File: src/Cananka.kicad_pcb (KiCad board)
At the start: 2 copper layers, 105.8 x 26 mm, 50 parts, among them J1 USB4085 B1HSW6, J2 MC 1,5/4, Q1 DMP3085, U1 FT230XS, U2 PIC18F25K80, U3 ISO1050, U4 PC817C, Y1 12 MHz

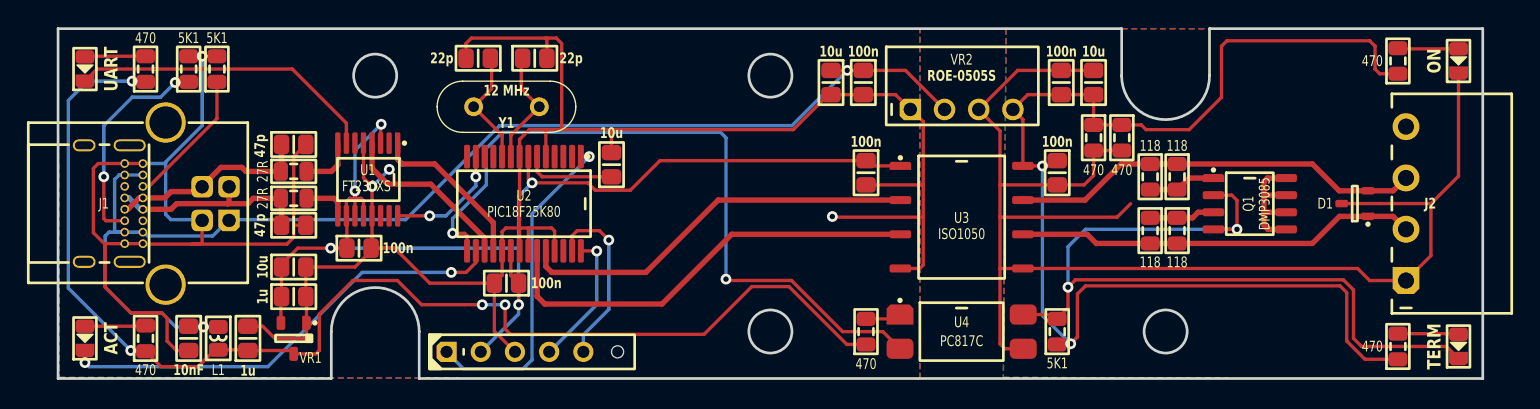
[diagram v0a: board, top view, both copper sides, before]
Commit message: Added soft-start circuit for DC-DC converter
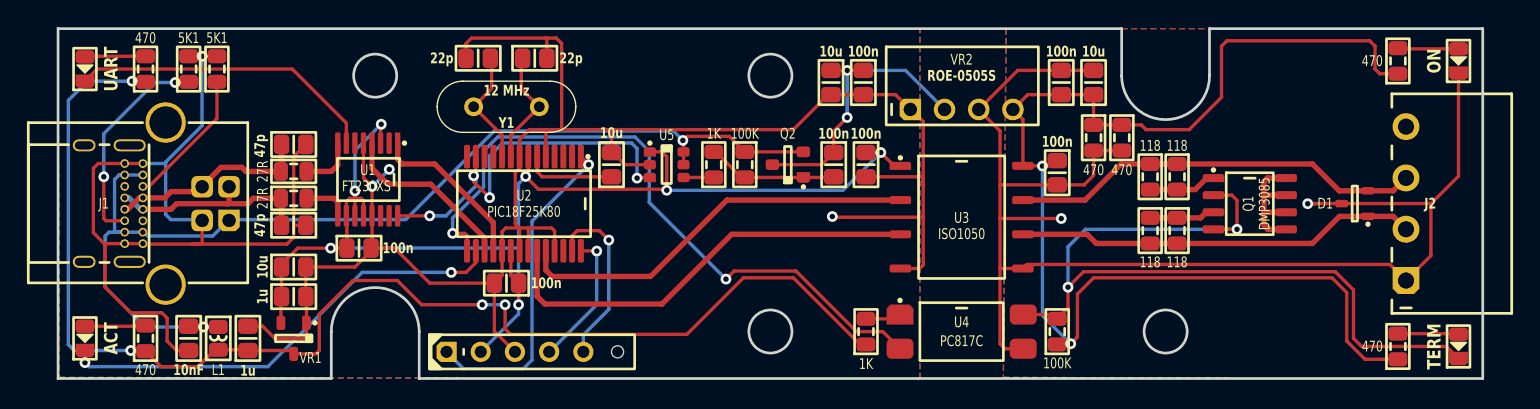
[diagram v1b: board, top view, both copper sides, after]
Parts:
- added C12: 100n, Medo64:C (0805), F.Cu at (77.6, 30.1)
- added Q2: Val**, Medo64:Q MOSFET-P (SOT23-3), F.Cu at (74.2, 30.1)
- added R14: 1K, Medo64:R (0805), F.Cu at (68.7, 30.1)
- added R18: 100K, Medo64:R (0805), F.Cu at (71.0, 30.1)
- added U5: 74LVC1T45, Medo64:U LevelTranslator [74LVC1T45] (SOT23-6), F.Cu at (65.2, 30.1)
- R17: renamed from R16; value 5K1 -> 100K
- R7: value 470 -> 1K
- moved C8 0.60 mm to (80.0, 30.1)
- renumbered C12 to C13, C13 to C14, C14 to C15, C15 to C16, C16 to C17, C17 to C18, R14 to R15, R15 to R16, R8 to R7, R9 to R8
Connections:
- C10 pad 1: A_5V_USB -> A_5V_SWITCHED
- C17 pad 1: A_5V_USB -> A_5V_SWITCHED
- VR2 pad 2: A_5V_USB -> A_5V_SWITCHED
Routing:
- net A_5V_SWITCHED: track 0.00 -> 22.3 mm, vias 0 -> 2
- net A_PWREN#: track 8.82 -> 28.7 mm, vias 2 -> 4
- net A_5V_USB: track 91.4 -> 79.4 mm
- net A_PWREN#_5V': track 0.00 -> 9.04 mm
- net A_3V3: track 86.9 -> 92.9 mm, vias 5 -> 7
- net A_GND: track 202.5 -> 206.4 mm
- net A_IO_TERMINATE#: track 53.6 -> 49.9 mm
- net A_5V: track 92.1 -> 94.6 mm
- net A_PWREN#_5V: track 0.00 -> 2.25 mm
- net B_GND: track 105.1 -> 102.9 mm, vias 0 -> 2
- net B_CAN_L_SPLIT: track 4.97 -> 4.44 mm

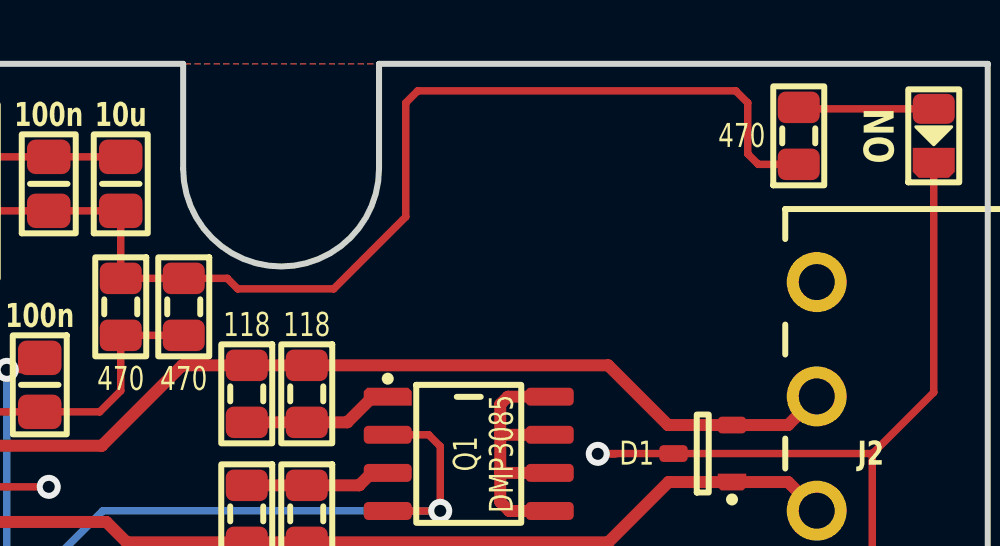
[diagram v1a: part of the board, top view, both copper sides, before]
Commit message: Added testing V+ output
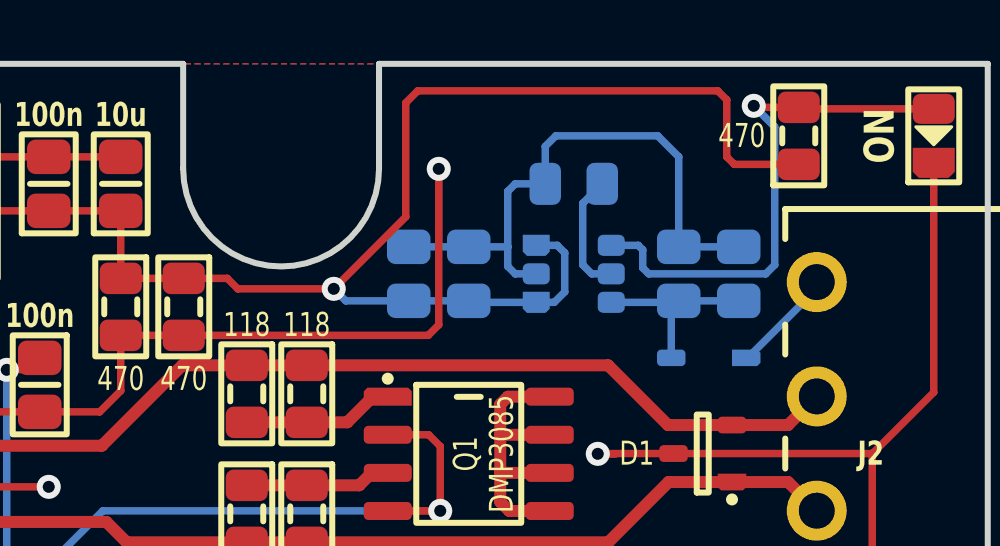
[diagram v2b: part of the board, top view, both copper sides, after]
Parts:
- added C101: 100n, Medo64:C (0805), B.Cu at (108.5, 27.0)
- added C102: 100n, Medo64:C (0805), B.Cu at (115.5, 27.0)
- added C103: 10u, Medo64:C (0805), B.Cu at (106.5, 27.0)
- added C104: 10u, Medo64:C (0805), B.Cu at (117.5, 27.0)
- added D101: CUS08F30, Medo64:D (SOD323), B.Cu at (116.5, 29.8)
- added R101: 300K, Medo64:R (0805), B.Cu at (112.0, 24.0)
- added U101: AP22653, Medo64:U LoadSwitch Adjustable [AP22653W6-7] (SOT23-6), B.Cu at (112.0, 27.0)
- renumbered R11 to R10, R12 to R11, R13 to R12, R7 to R13, R10 to R9
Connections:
- J2 pad 4: (no net) -> B_5V_DIODED
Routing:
- net B_GND: track 102.9 -> 138.7 mm, vias 2 -> 3
- net B_LED_POWER: track 4.45 -> 17.9 mm, vias 0 -> 1
- net B_5V: track 93.2 -> 103.7 mm, vias 2 -> 3
- net B_5V_OUT: track 0.00 -> 6.27 mm
- net B_5V_DIODED: track 0.00 -> 4.41 mm
- net B_ILIMIT: track 0.00 -> 4.04 mm

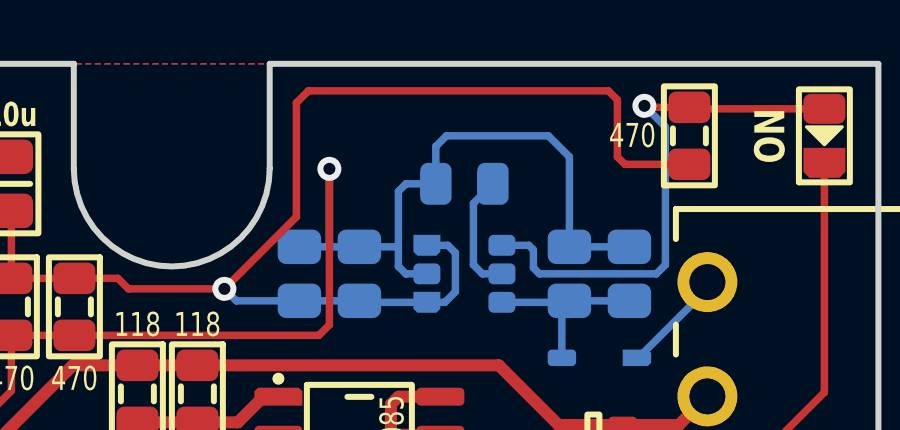
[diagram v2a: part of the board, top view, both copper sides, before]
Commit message: Added assembly title
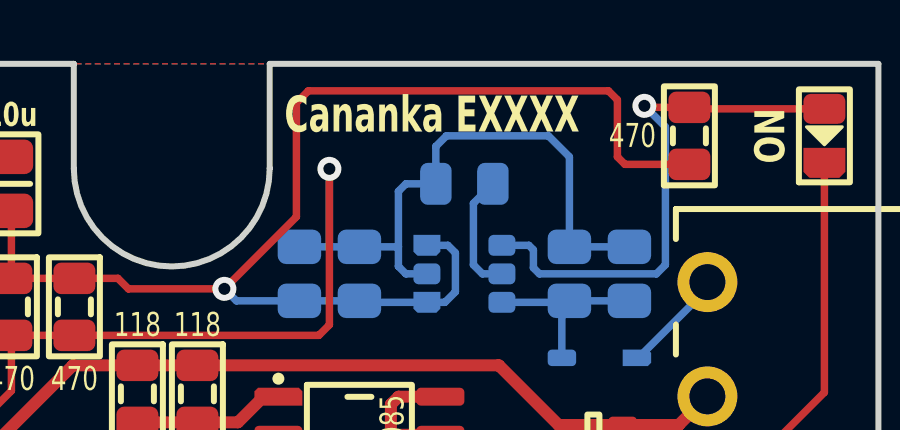
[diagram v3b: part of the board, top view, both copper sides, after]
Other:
- board text added: "Cananka EXXXX"
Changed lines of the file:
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@@
 		(layer "Margin")
+	)
+	(gr_text "Cananka EXXXX"
+		(at 106 21 0)
+		(layer "F.SilkS")
+		(effects
+			(font
+				(size 1.2 0.8)
+				(thickness 0.2)
+				(bold yes)
+			)
+			(justify left top)
+		)
 	)
 	(segment

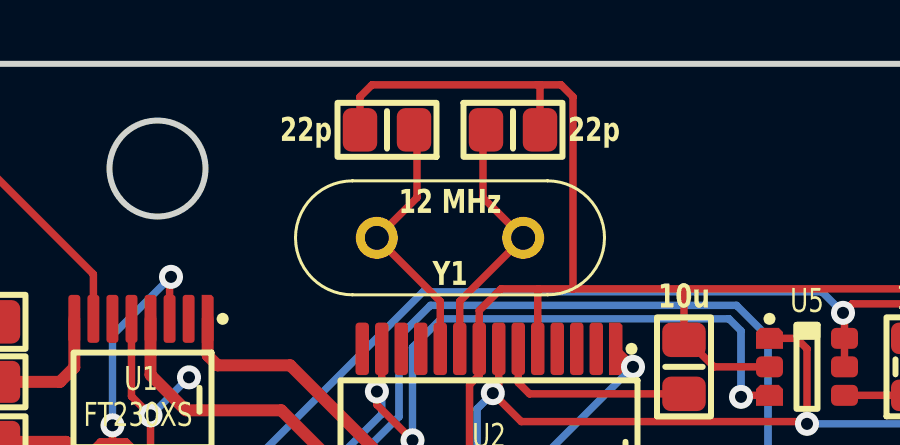
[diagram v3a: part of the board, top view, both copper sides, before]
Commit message: Updated crystal circuit
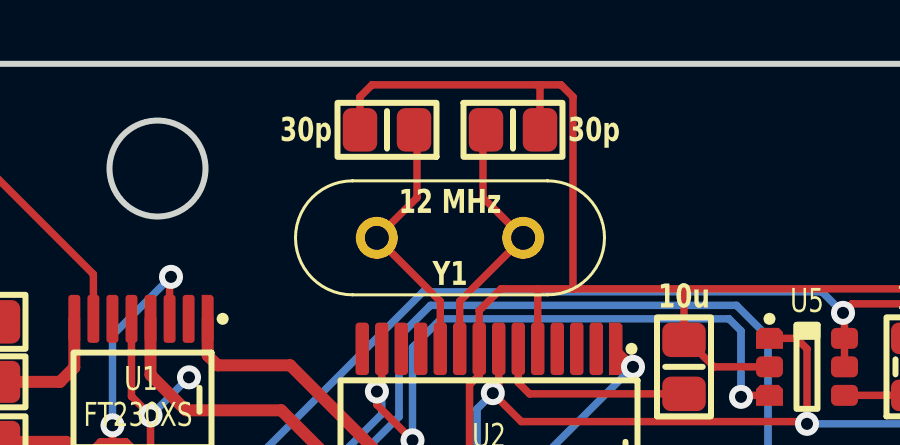
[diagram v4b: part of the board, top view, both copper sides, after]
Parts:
- C1, C2: value 22p -> 30p
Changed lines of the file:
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@@
 			)
 		)
-		(property "Value" "22p"
+		(property "Value" "30p"
 			(at 2.7 0 0)
 			(layer "F.SilkS")
@@
 			)
 		)
-		(property "Value" "22p"
+		(property "Value" "30p"
 			(at 2.7 0 0)
 			(layer "F.SilkS")

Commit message: Updated refdes
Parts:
- U4: renamed from U5; value 74LVC1T45 -> 74LVC1T45
- renumbered U4 to AT1
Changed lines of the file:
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@@
 		(at 87.1 42.5)
 		(tags "SOIC127P600X170-9N")
-		(property "Reference" "U4"
+		(property "Reference" "AT1"
 			(at 0 -0.7 0)
 			(layer "F.SilkS")
@@
 		(at 65.2 30.1)
 		(descr "Diodes 74LVC1T45W6-7")
-		(property "Reference" "U5"
+		(property "Reference" "U4"
 			(at 0 -2.2 0)
 			(layer "F.SilkS")
@@
 			)
 		)
-		(property "Value" "  74LVC1T45"
+		(property "Value" " 74LVC1T45"
 			(at 0 2.4 180)
 			(layer "F.SilkS")

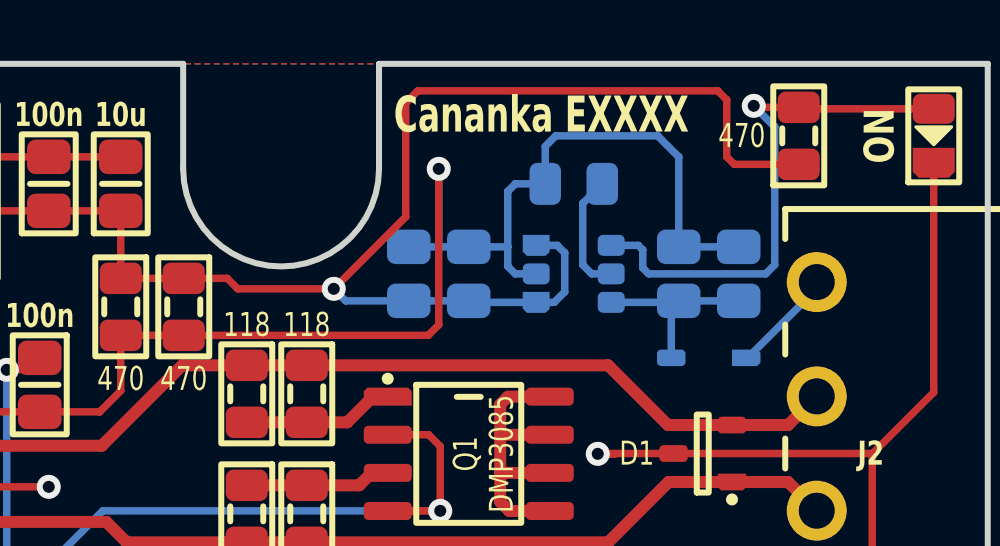
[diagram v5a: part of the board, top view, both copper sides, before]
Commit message: Removed external power supply
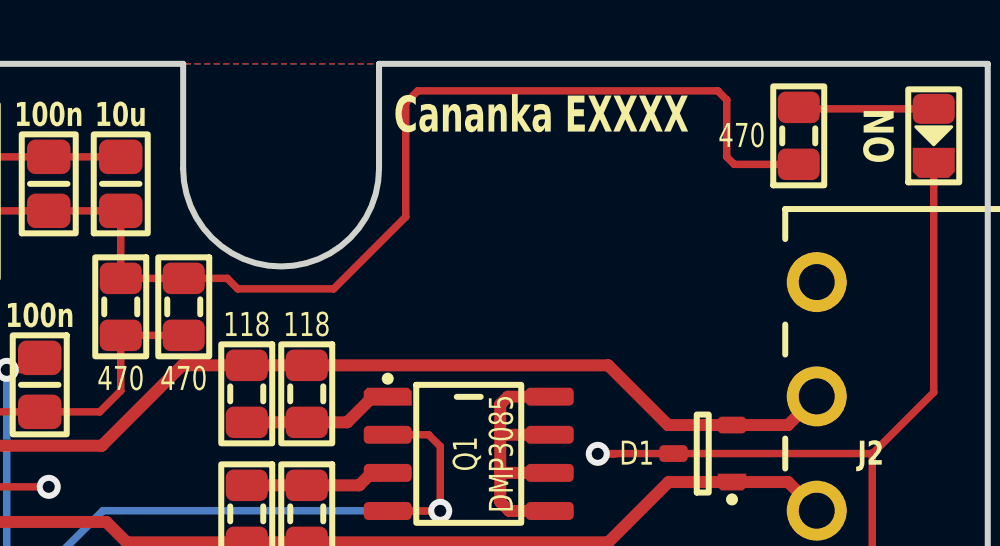
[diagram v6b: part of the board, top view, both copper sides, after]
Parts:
- removed C101, C102: 100n, Medo64:C (0805)
- removed C103, C104: 10u, Medo64:C (0805)
- removed D101: CUS08F30, Medo64:D (SOD323)
- removed R101: 300K, Medo64:R (0805)
- removed U101: AP22653, Medo64:U LoadSwitch Adjustable [AP22653W6-7] (SOT23-6)
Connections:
- J2 pad 4: B_5V_DIODED -> (no net)
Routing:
- net B_GND: track 138.7 -> 102.9 mm, vias 3 -> 2
- net B_LED_POWER: track 17.9 -> 4.45 mm, vias 1 -> 0
- net B_5V: track 103.7 -> 93.3 mm, vias 3 -> 2
- net B_5V_OUT: track 6.27 -> 0.00 mm
- net B_5V_DIODED: track 4.41 -> 0.00 mm
- net B_ILIMIT: track 4.04 -> 0.00 mm

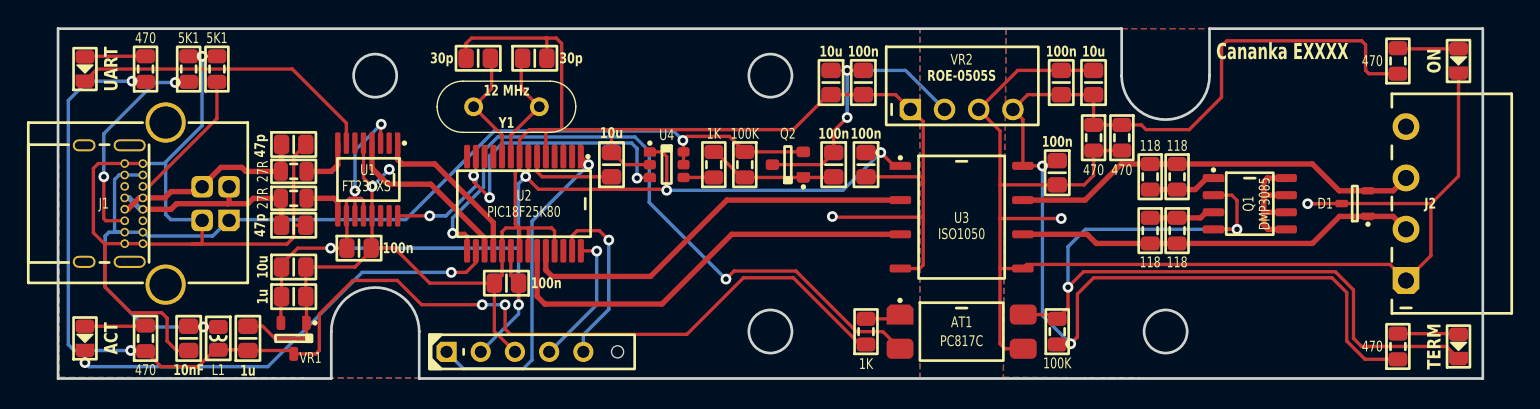
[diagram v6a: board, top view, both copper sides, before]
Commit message: Fixed pwren# line behavior
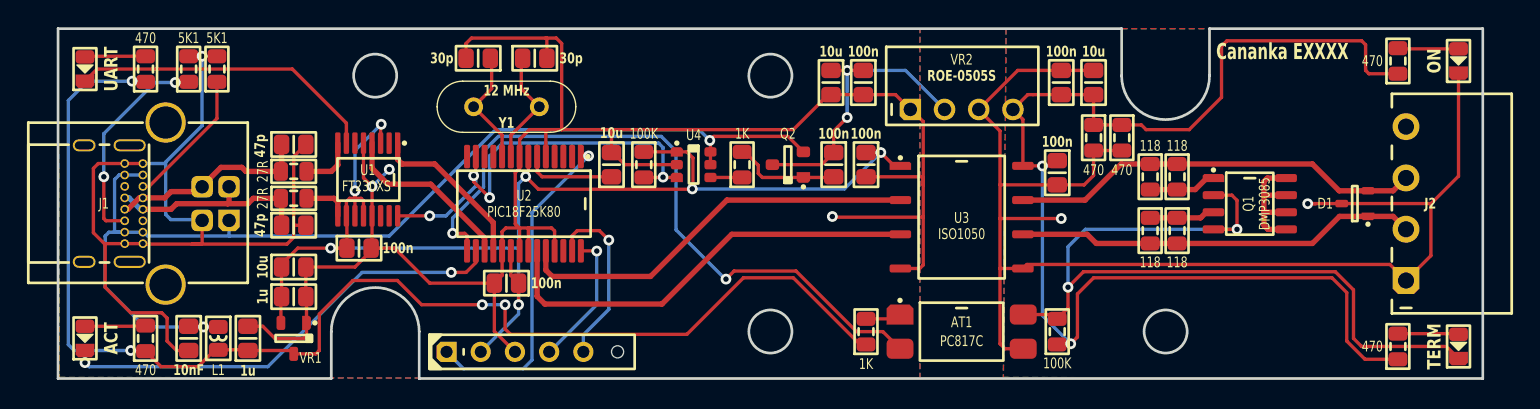
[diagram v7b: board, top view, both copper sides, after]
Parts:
- moved R18 7.50 mm to (63.5, 30.1)
- moved R14 2.10 mm to (70.8, 30.1)
- moved U4 2.00 mm to (67.2, 30.1)
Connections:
- R18 pad 1: A_5V_USB -> A_3V3
- R18 pad 2: A_PWREN#_5V' -> A_PWREN#
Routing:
- net A_PWREN#: track 28.7 -> 32.1 mm
- net A_3V3: track 92.9 -> 95.1 mm
- net A_GND: track 206.4 -> 208.4 mm
- net A_5V_USB: track 79.4 -> 80.6 mm
- net A_IO_TERMINATE#: track 49.9 -> 51.1 mm
- net A_PWREN#_5V': track 9.04 -> 7.96 mm

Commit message: Fixing termination MOSFET connections
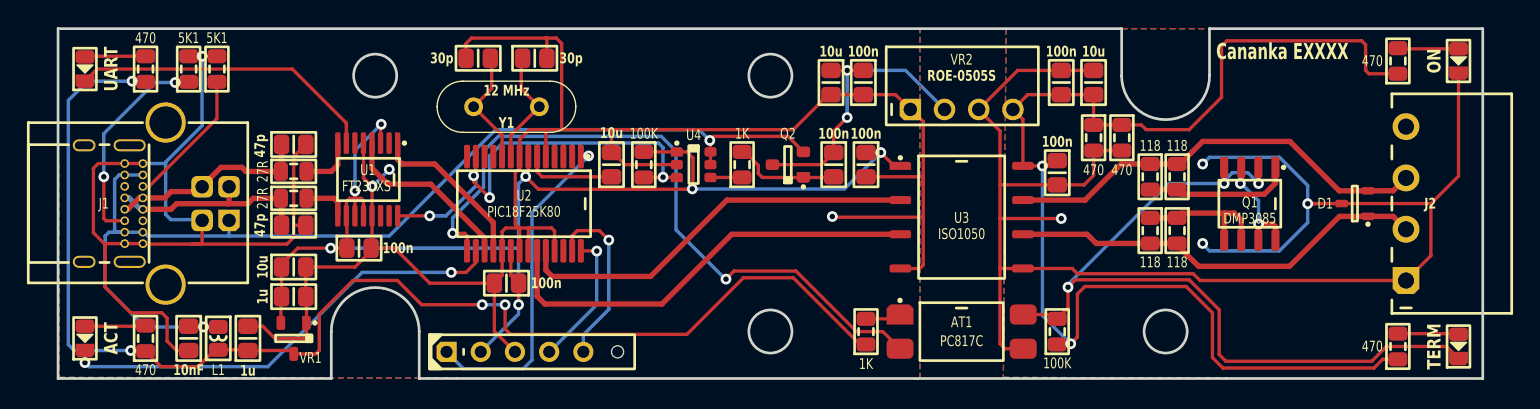
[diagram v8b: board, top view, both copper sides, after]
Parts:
- Q2: value Val** -> BSS84
- turned Q1 to -90 degrees
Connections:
- net B_CAN_H_SPLIT renamed B_CAN_H_TERM
- Q1 pad 3: B_CAN_L_SPLIT -> B_CAN_I_TERM
- Q1 pad 5: B_CAN_SPLIT -> B_CAN_L_TERM
- Q1 pad 6: B_CAN_SPLIT -> B_CAN_L_TERM
- Q1 pad 7: B_CAN_SPLIT -> B_CAN_I_TERM
- Q1 pad 8: B_CAN_SPLIT -> B_CAN_I_TERM
- R5 pad 1: B_CAN_L_SPLIT -> B_CAN_L_TERM
- R6 pad 1: B_CAN_L_SPLIT -> B_CAN_L_TERM
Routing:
- net B_GND: track 102.9 -> 123.2 mm, vias 2 -> 4
- net B_CAN_L_TERM: track 0.00 -> 10.7 mm
- net B_CAN_SPLIT: track 10.1 -> 0.00 mm
- net B_CAN_I_TERM: track 0.00 -> 8.28 mm, vias 0 -> 2
- net B_CAN_H_TERM: track 4.51 -> 11.0 mm
- net B_CAN_L_SPLIT: track 4.44 -> 0.00 mm
- net B_CAN_L: track 30.0 -> 31.4 mm
- net B_CAN_H: track 30.8 -> 31.9 mm
- net B_IO_TERMINATE#: track 61.6 -> 60.6 mm, vias 2 -> 3
